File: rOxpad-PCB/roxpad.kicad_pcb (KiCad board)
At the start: 2 copper layers, 66 x 53 mm, 8 parts

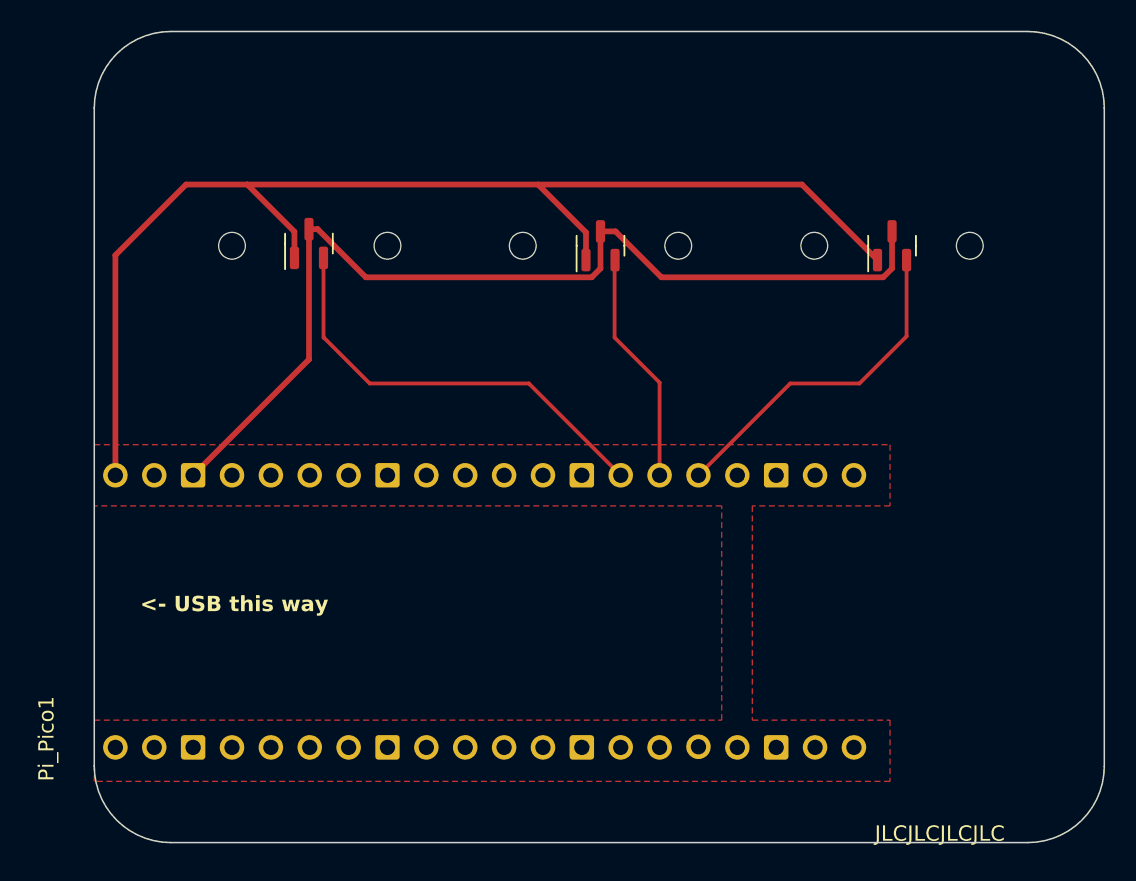
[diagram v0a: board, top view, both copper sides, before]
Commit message: fix pinout (thanks Bexin!)
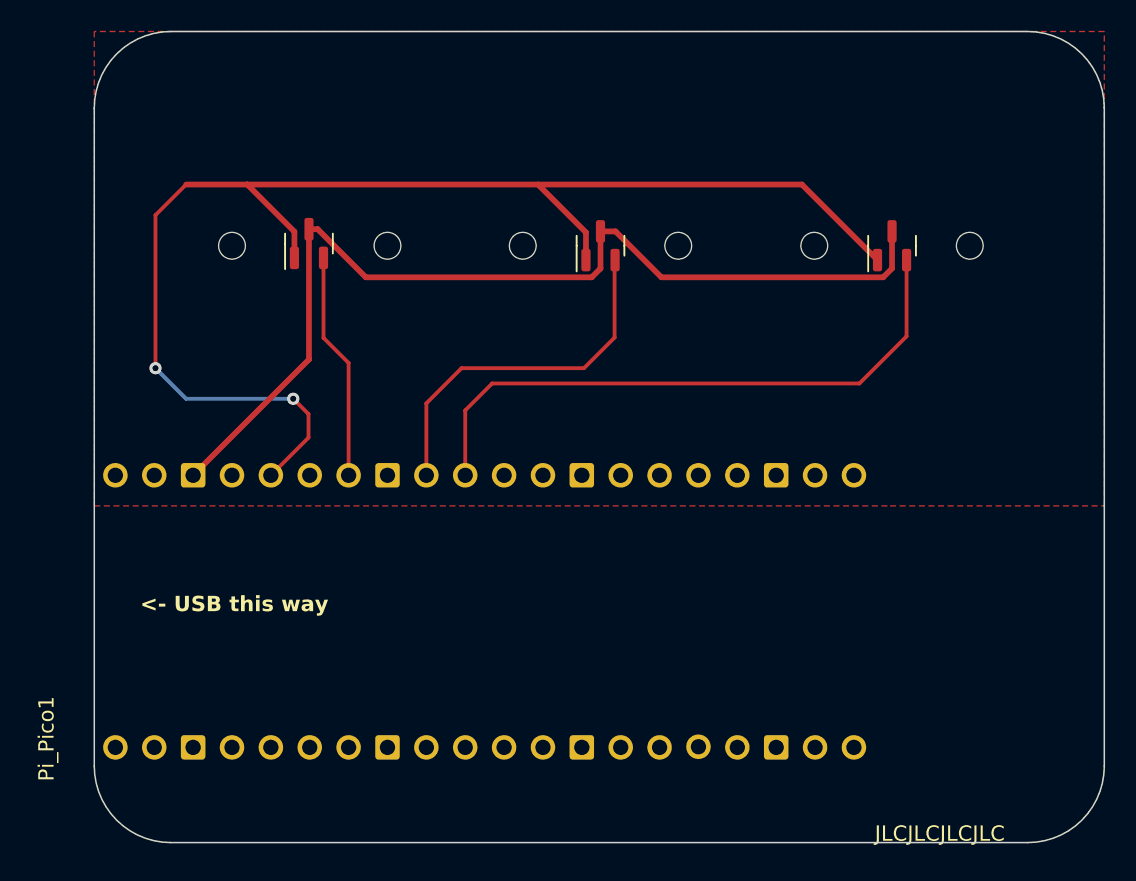
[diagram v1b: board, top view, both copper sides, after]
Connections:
- Pi_Pico1 pad 25: Net-(Pi_Pico1-GP19) -> unconnected-(Pi_Pico1-GP19-Pad25)
- Pi_Pico1 pad 26: Net-(Middle_Sensor1-OUT) -> unconnected-(Pi_Pico1-GP20-Pad26)
- Pi_Pico1 pad 27: Net-(Left_sensor1-OUT) -> unconnected-(Pi_Pico1-GP21-Pad27)
- Pi_Pico1 pad 31: unconnected-(Pi_Pico1-GP26-Pad31) -> Net-(Pi_Pico1-GP26)
- Pi_Pico1 pad 32: unconnected-(Pi_Pico1-GP27-Pad32) -> Net-(Middle_Sensor1-OUT)
- Pi_Pico1 pad 34: unconnected-(Pi_Pico1-GP28-Pad34) -> Net-(Left_sensor1-OUT)
- Pi_Pico1 pad 36: unconnected-(Pi_Pico1-3V3_OUT-Pad36) -> Net-(Left_sensor1-VDD)
- Pi_Pico1 pad 40: Net-(Left_sensor1-VDD) -> unconnected-(Pi_Pico1-VBUS-Pad40)
- Right_Sensor1 pad 2: Net-(Pi_Pico1-GP19) -> Net-(Pi_Pico1-GP26)
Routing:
- net Net-(Pi_Pico1-GP26): track 0.00 -> 40.1 mm
- net Net-(Pi_Pico1-GP19): track 22.3 -> 0.00 mm
- net Net-(Left_sensor1-OUT): track 28.4 -> 14.9 mm
- net Net-(Middle_Sensor1-OUT): track 15.3 -> 23.9 mm
- net Net-(Left_sensor1-VDD): track 80.4 -> 88.6 mm, vias 0 -> 2
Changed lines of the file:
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@@
   (net 30 "unconnected-(Pi_Pico1-GP22-Pad29)")
   (net 31 "unconnected-(Pi_Pico1-RUN-Pad30)")
-  (net 32 "unconnected-(Pi_Pico1-GP26-Pad31)")
-  (net 33 "unconnected-(Pi_Pico1-GP27-Pad32)")
+  (net 32 "unconnected-(Pi_Pico1-GP19-Pad25)")
+  (net 33 "unconnected-(Pi_Pico1-GP20-Pad26)")
   (net 34 "unconnected-(Pi_Pico1-AGND-Pad33)")
-  (net 35 "unconnected-(Pi_Pico1-GP28-Pad34)")
+  (net 35 "unconnected-(Pi_Pico1-GP21-Pad27)")
   (net 36 "unconnected-(Pi_Pico1-ADC_VREF-Pad35)")
-  (net 37 "unconnected-(Pi_Pico1-3V3_OUT-Pad36)")
-  (net 38 "Net-(Pi_Pico1-GP19)")
-  (net 39 "unconnected-(Pi_Pico1-VSYS-Pad39)")
+  (net 37 "Net-(Pi_Pico1-GP26)")
+  (net 38 "unconnected-(Pi_Pico1-VSYS-Pad39)")
+  (net 39 "unconnected-(Pi_Pico1-VBUS-Pad40)")
   (net 40 "unconnected-(Pi_Pico1-3V3_EN-Pad37)")
   (footprint "marbastlib-mx:SW_MX_1u_lekker" (layer "F.Cu")
@@
       (net 25 "unconnected-(Pi_Pico1-GP18-Pad24)") (pinfunction "GP18") (pintype "bidirectional"))
     (pad "25" thru_hole circle (at 8.89 13.97 90) (size 1.6 1.6) (drill 1) (layers "*.Cu" "*.Mask")
-      (net 38 "Net-(Pi_Pico1-GP19)") (pinfunction "GP19") (pintype "bidirectional"))
+      (net 32 "unconnected-(Pi_Pico1-GP19-Pad25)") (pinfunction "GP19") (pintype "bidirectional"))
     (pad "26" thru_hole circle (at 8.89 11.43 90) (size 1.6 1.6) (drill 1) (layers "*.Cu" "*.Mask")
-      (net 4 "Net-(Middle_Sensor1-OUT)") (pinfunction "GP20") (pintype "bidirectional"))
+      (net 33 "unconnected-(Pi_Pico1-GP20-Pad26)") (pinfunction "GP20") (pintype "bidirectional"))
     (pad "27" thru_hole circle (at 8.89 8.89 90) (size 1.6 1.6) (drill 1) (layers "*.Cu" "*.Mask")
-      (net 2 "Net-(Left_sensor1-OUT)") (pinfunction "GP21") (pintype "bidirectional"))
+      (net 35 "unconnected-(Pi_Pico1-GP21-Pad27)") (pinfunction "GP21") (pintype "bidirectional"))
     (pad "28" thru_hole roundrect (at 8.89 6.35 90) (size 1.6 1.6) (drill 1) (layers "*.Cu" "*.Mask") (roundrect_rratio 0.125)
       (net 29 "unconnected-(Pi_Pico1-GND-Pad28)") (pinfunction "GND") (pintype "power_in"))
@@
       (net 31 "unconnected-(Pi_Pico1-RUN-Pad30)") (pinfunction "RUN") (pintype "input"))
     (pad "31" thru_hole circle (at 8.89 -1.27 90) (size 1.6 1.6) (drill 1) (layers "*.Cu" "*.Mask")
-      (net 32 "unconnected-(Pi_Pico1-GP26-Pad31)") (pinfunction "GP26") (pintype "bidirectional"))
+      (net 37 "Net-(Pi_Pico1-GP26)") (pinfunction "GP26") (pintype "bidirectional"))
     (pad "32" thru_hole circle (at 8.89 -3.81 90) (size 1.6 1.6) (drill 1) (layers "*.Cu" "*.Mask")
-      (net 33 "unconnected-(Pi_Pico1-GP27-Pad32)") (pinfunction "GP27") (pintype "bidirectional"))
+      (net 4 "Net-(Middle_Sensor1-OUT)") (pinfunction "GP27") (pintype "bidirectional"))
     (pad "33" thru_hole roundrect (at 8.89 -6.35 90) (size 1.6 1.6) (drill 1) (layers "*.Cu" "*.Mask") (roundrect_rratio 0.125)
       (net 34 "unconnected-(Pi_Pico1-AGND-Pad33)") (pinfunction "AGND") (pintype "power_in"))
     (pad "34" thru_hole circle (at 8.89 -8.89 90) (size 1.6 1.6) (drill 1) (layers "*.Cu" "*.Mask")
-      (net 35 "unconnected-(Pi_Pico1-GP28-Pad34)") (pinfunction "GP28") (pintype "bidirectional"))
+      (net 2 "Net-(Left_sensor1-OUT)") (pinfunction "GP28") (pintype "bidirectional"))
     (pad "35" thru_hole circle (at 8.89 -11.43 90) (size 1.6 1.6) (drill 1) (layers "*.Cu" "*.Mask")
       (net 36 "unconnected-(Pi_Pico1-ADC_VREF-Pad35)") (pinfunction "ADC_VREF") (pintype "power_in"))
     (pad "36" thru_hole circle (at 8.89 -13.97 90) (size 1.6 1.6) (drill 1) (layers "*.Cu" "*.Mask")
-      (net 37 "unconnected-(Pi_Pico1-3V3_OUT-Pad36)") (pinfunction "3V3_OUT") (pintype "power_in"))
+      (net 1 "Net-(Left_sensor1-VDD)") (pinfunction "3V3_OUT") (pintype "power_in"))
     (pad "37" thru_hole circle (at 8.89 -16.51 90) (size 1.6 1.6) (drill 1) (layers "*.Cu" "*.Mask")
       (net 40 "unconnected-(Pi_Pico1-3V3_EN-Pad37)") (pinfunction "3V3_EN") (pintype "input"))
@@
       (net 3 "Net-(Left_sensor1-GND)") (pinfunction "GND") (pintype "power_in"))
     (pad "39" thru_hole circle (at 8.89 -21.59 90) (size 1.6 1.6) (drill 1) (layers "*.Cu" "*.Mask")
-      (net 39 "unconnected-(Pi_Pico1-VSYS-Pad39)") (pinfunction "VSYS") (pintype "free"))
+      (net 38 "unconnected-(Pi_Pico1-VSYS-Pad39)") (pinfunction "VSYS") (pintype "free"))
     (pad "40" thru_hole circle (at 8.89 -24.13 90) (size 1.6 1.6) (drill 1) (layers "*.Cu" "*.Mask")
-      (net 1 "Net-(Left_sensor1-VDD)") (pinfunction "VBUS") (pintype "free"))
+      (net 39 "unconnected-(Pi_Pico1-VBUS-Pad40)") (pinfunction "VBUS") (pintype "free"))
     (model "${KICAD6_3DMODEL_USER_DIR}/RPi Pico w_headers.step"
       (offset (xyz 0 0 9))
@@
       (net 1 "Net-(Left_sensor1-VDD)") (pinfunction "VDD") (pintype "power_in"))
     (pad "2" smd roundrect (at -0.9375 0.95 90) (size 1.475 0.6) (layers "F.Cu" "F.Paste" "F.Mask") (roundrect_rratio 0.25)
-      (net 38 "Net-(Pi_Pico1-GP19)") (pinfunction "OUT") (pintype "output"))
+      (net 37 "Net-(Pi_Pico1-GP26)") (pinfunction "OUT") (pintype "output"))
     (pad "3" smd roundrect (at 0.9375 0 90) (size 1.475 0.6) (layers "F.Cu" "F.Paste" "F.Mask") (roundrect_rratio 0.25)
       (net 3 "Net-(Left_sensor1-GND)") (pinfunction "GND") (pintype "power_in"))
@@
     (effects (font (size 1 1) (thickness 0.15)) (justify left bottom))
   )
+  (segment (start 163 56) (end 163 66) (width 0.25) (layer "F.Cu") (net 1))
+  (segment (start 172 68) (end 173 69) (width 0.25) (layer "F.Cu") (net 1))
   (segment (start 169 54) (end 205.2425 54) (width 0.375) (layer "F.Cu") (net 1))
+  (segment (start 165 54) (end 163 56) (width 0.25) (layer "F.Cu") (net 1))
   (segment (start 191.13 57.13) (end 188 54) (width 0.375) (layer "F.Cu") (net 1))
   (segment (start 172.08 57.08) (end 169 54) (width 0.375) (layer "F.Cu") (net 1))
   (segment (start 165 54) (end 169 54) (width 0.375) (layer "F.Cu") (net 1))
-  (segment (start 160.38 73) (end 160.38 58.62) (width 0.375) (layer "F.Cu") (net 1))
-  (segment (start 160.38 58.62) (end 165 54) (width 0.375) (layer "F.Cu") (net 1))
   (segment (start 191.13 58.9375) (end 191.13 57.13) (width 0.375) (layer "F.Cu") (net 1))
   (segment (start 172.08 58.793749) (end 172.08 57.08) (width 0.375) (layer "F.Cu") (net 1))
+  (segment (start 173 69) (end 173 70.54) (width 0.25) (layer "F.Cu") (net 1))
   (segment (start 205.2425 54) (end 210.18 58.9375) (width 0.375) (layer "F.Cu") (net 1))
-  (segment (start 193.4 73) (end 187.4 67) (width 0.25) (layer "F.Cu") (net 2))
+  (segment (start 173 70.54) (end 170.54 73) (width 0.25) (layer "F.Cu") (net 1))
+  (via (at 163 66) (size 0.8) (drill 0.4) (layers "F.Cu" "B.Cu") (net 1))
+  (via (at 172 68) (size 0.8) (drill 0.4) (layers "F.Cu" "B.Cu") (net 1))
+  (segment (start 163 66) (end 165 68) (width 0.25) (layer "B.Cu") (net 1))
+  (segment (start 165 68) (end 172 68) (width 0.25) (layer "B.Cu") (net 1))
   (segment (start 173.98 58.793749) (end 173.98 64.02) (width 0.25) (layer "F.Cu") (net 2))
-  (segment (start 177 67) (end 174 64) (width 0.25) (layer "F.Cu") (net 2))
-  (segment (start 187.4 67) (end 177 67) (width 0.25) (layer "F.Cu") (net 2))
+  (segment (start 173.98 64.02) (end 175.62 65.66) (width 0.25) (layer "F.Cu") (net 2))
+  (segment (start 175.62 65.66) (end 175.62 73) (width 0.25) (layer "F.Cu") (net 2))
   (segment (start 211.13 57.0625) (end 211.13 59.48514) (width 0.375) (layer "F.Cu") (net 3))
   (segment (start 173.03 56.918749) (end 173.03 65.43) (width 0.375) (layer "F.Cu") (net 3))
@@
   (segment (start 173.60264 56.918749) (end 173.03 56.918749) (width 0.375) (layer "F.Cu") (net 3))
   (segment (start 191.50264 60.0625) (end 176.746391 60.0625) (width 0.375) (layer "F.Cu") (net 3))
+  (segment (start 191 66) (end 183 66) (width 0.25) (layer "F.Cu") (net 4))
   (segment (start 193 58.9675) (end 193 64) (width 0.25) (layer "F.Cu") (net 4))
   (segment (start 193.03 58.9375) (end 193 58.9675) (width 0.25) (layer "F.Cu") (net 4))
-  (segment (start 195.94 73) (end 195.94 66.94) (width 0.25) (layer "F.Cu") (net 4))
-  (segment (start 195.94 66.94) (end 193 64) (width 0.25) (layer "F.Cu") (net 4))
-  (segment (start 204.48 67) (end 198.48 73) (width 0.25) (layer "F.Cu") (net 38))
-  (segment (start 212.08 58.9375) (end 212.08 63.92) (width 0.25) (layer "F.Cu") (net 38))
-  (segment (start 209 67) (end 204.48 67) (width 0.25) (layer "F.Cu") (net 38))
-  (segment (start 212.08 63.92) (end 209 67) (width 0.25) (layer "F.Cu") (net 38))
+  (segment (start 180.7 68.3) (end 180.7 73) (width 0.25) (layer "F.Cu") (net 4))
+  (segment (start 183 66) (end 180.7 68.3) (width 0.25) (layer "F.Cu") (net 4))
+  (segment (start 193 64) (end 191 66) (width 0.25) (layer "F.Cu") (net 4))
+  (segment (start 209 67) (end 185 67) (width 0.25) (layer "F.Cu") (net 37))
+  (segment (start 185 67) (end 183.24 68.76) (width 0.25) (layer "F.Cu") (net 37))
+  (segment (start 212.08 63.92) (end 209 67) (width 0.25) (layer "F.Cu") (net 37))
+  (segment (start 183.24 68.76) (end 183.24 73) (width 0.25) (layer "F.Cu") (net 37))
+  (segment (start 212.08 58.9375) (end 212.08 63.92) (width 0.25) (layer "F.Cu") (net 37))
   (zone (net 3) (net_name "Net-(Left_sensor1-GND)") (layer "F.Cu") (hatch edge 0.5)
     (connect_pads (clearance 0.5))
     (min_thickness 0.25) (filled_areas_thickness no)
-    (fill (thermal_gap 0.5) (thermal_bridge_width 0.5))
+    (fill yes (thermal_gap 0.5) (thermal_bridge_width 0.5))
     (polygon
       (pts
-        (xy 159 71)
-        (xy 211 71)
+        (xy 159 75)
         (xy 211 75)
-        (xy 202 75)
-        (xy 202 89)
-        (xy 211 89)
-        (xy 211 93)
-        (xy 159 93)
-        (xy 159 89)
-        (xy 200 89)
-        (xy 200 75)
-        (xy 159 75)
-      )
-    )
+        (xy 225 75)
+        (xy 225 71)
+        (xy 225 44)
+        (xy 159 44)
+      )
+    )

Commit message: change ' hall sensor`to proper sensor name
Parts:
- Left_sensor1, Middle_Sensor1, Right_Sensor1: value Hall_Sensor -> SS49E
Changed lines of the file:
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@@
         (effects (font (size 1 1) (thickness 0.15)))
     )
-    (fp_text value "Hall_Sensor" (at 0 2.4 90) (layer "F.Fab")
+    (fp_text value "SS49E" (at 0 2.4 90) (layer "F.Fab")
         (effects (font (size 1 1) (thickness 0.15)))
     )
@@
         (effects (font (size 1 1) (thickness 0.15)))
     )
-    (fp_text value "Hall_Sensor" (at 0 2.4 90) (layer "F.Fab")
+    (fp_text value "SS49E" (at 0 2.4 90) (layer "F.Fab")
         (effects (font (size 1 1) (thickness 0.15)))
     )
@@
         (effects (font (size 1 1) (thickness 0.15)))
     )
-    (fp_text value "Hall_Sensor" (at 0 2.4 90) (layer "F.Fab")
+    (fp_text value "SS49E" (at 0 2.4 90) (layer "F.Fab")
         (effects (font (size 1 1) (thickness 0.15)))
     )
@@
     (effects (font (size 1 1) (thickness 0.15)) (justify left bottom))
   )
+  (dimension (type aligned) (layer "Cmts.User")
+    (pts (xy 170 97) (xy 170 44))
+    (height -19)
+    (gr_text "53.0000 mm" (at 149.2 70.5 90) (layer "Cmts.User")
+      (effects (font (size 1.5 1.5) (thickness 0.3)))
+    )
+    (format (prefix "") (suffix "") (units 3) (units_format 1) (precision 4))
+    (style (thickness 0.2) (arrow_length 1.27) (text_position_mode 0) (extension_height 0.58642) (extension_offset 0.5) keep_text_aligned)
+  )
+  (dimension (type aligned) (layer "Cmts.User")
+    (pts (xy 163.555 58) (xy 220.655 58))
+    (height -11)
+    (gr_text "57.1000 mm" (at 192.105 45.2) (layer "Cmts.User")
+      (effects (font (size 1.5 1.5) (thickness 0.3)))
+    )
+    (format (prefix "") (suffix "") (units 3) (units_format 1) (precision 4))
+    (style (thickness 0.2) (arrow_length 1.27) (text_position_mode 0) (extension_height 0.58642) (extension_offset 0.5) keep_text_aligned)
+  )
+  (dimension (type aligned) (layer "Cmts.User")
+    (pts (xy 159 50) (xy 225 50))
+    (height -13)
+    (gr_text "66.0000 mm" (at 192 35.85) (layer "Cmts.User")
+      (effects (font (size 1 1) (thickness 0.15)))
+    )
+    (format (prefix "") (suffix "") (units 3) (units_format 1) (precision 4))
+    (style (thickness 0.15) (arrow_length 1.27) (text_position_mode 0) (extension_height 0.58642) (extension_offset 0.5) keep_text_aligned)
+  )
   (segment (start 163 56) (end 163 66) (width 0.25) (layer "F.Cu") (net 1))

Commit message: changed designations
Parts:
- renumbered Left_sensor1 to H1, Middle_Sensor1 to H2, Right_Sensor1 to H3
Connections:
- Pi_Pico1 pad 31: Net-(Pi_Pico1-GP26) -> Net-(H3-OUT)
- Pi_Pico1 pad 32: Net-(Middle_Sensor1-OUT) -> Net-(H2-OUT)
- Pi_Pico1 pad 34: Net-(Left_sensor1-OUT) -> Net-(H1-OUT)
- Pi_Pico1 pad 36: Net-(Left_sensor1-VDD) -> Net-(H1-VDD)
- Pi_Pico1 pad 38: Net-(Left_sensor1-GND) -> Net-(H1-GND)
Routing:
- added copper zone on F.Cu, net Net-(H1-GND)
- removed copper zone on F.Cu, net Net-(Left_sensor1-GND)
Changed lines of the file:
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@@
       (outputformat 1)
       (mirror false)
-      (drillshape 1)
+      (drillshape 0)
       (scaleselection 1)
-      (outputdirectory "")
+      (outputdirectory "gerber/")
     )
   )
@@
   (net 39 "unconnected-(Pi_Pico1-VBUS-Pad40)")
   (net 40 "unconnected-(Pi_Pico1-3V3_EN-Pad37)")
+  (net 41 "Net-(H1-VDD)")
+  (net 42 "Net-(H1-OUT)")
+  (net 43 "Net-(H1-GND)")
+  (net 44 "Net-(H2-OUT)")
+  (net 45 "Net-(H3-OUT)")
   (footprint "marbastlib-mx:SW_MX_1u_lekker" (layer "F.Cu")
     (at 173.08 58)
@@
       (net 31 "unconnected-(Pi_Pico1-RUN-Pad30)") (pinfunction "RUN") (pintype "input"))
     (pad "31" thru_hole circle (at 8.89 -1.27 90) (size 1.6 1.6) (drill 1) (layers "*.Cu" "*.Mask")
-      (net 37 "Net-(Pi_Pico1-GP26)") (pinfunction "GP26") (pintype "bidirectional"))
+      (net 45 "Net-(H3-OUT)") (pinfunction "GP26") (pintype "bidirectional"))
     (pad "32" thru_hole circle (at 8.89 -3.81 90) (size 1.6 1.6) (drill 1) (layers "*.Cu" "*.Mask")
-      (net 4 "Net-(Middle_Sensor1-OUT)") (pinfunction "GP27") (pintype "bidirectional"))
+      (net 44 "Net-(H2-OUT)") (pinfunction "GP27") (pintype "bidirectional"))
     (pad "33" thru_hole roundrect (at 8.89 -6.35 90) (size 1.6 1.6) (drill 1) (layers "*.Cu" "*.Mask") (roundrect_rratio 0.125)
       (net 34 "unconnected-(Pi_Pico1-AGND-Pad33)") (pinfunction "AGND") (pintype "power_in"))
     (pad "34" thru_hole circle (at 8.89 -8.89 90) (size 1.6 1.6) (drill 1) (layers "*.Cu" "*.Mask")
-      (net 2 "Net-(Left_sensor1-OUT)") (pinfunction "GP28") (pintype "bidirectional"))
+      (net 42 "Net-(H1-OUT)") (pinfunction "GP28") (pintype "bidirectional"))
     (pad "35" thru_hole circle (at 8.89 -11.43 90) (size 1.6 1.6) (drill 1) (layers "*.Cu" "*.Mask")
       (net 36 "unconnected-(Pi_Pico1-ADC_VREF-Pad35)") (pinfunction "ADC_VREF") (pintype "power_in"))
     (pad "36" thru_hole circle (at 8.89 -13.97 90) (size 1.6 1.6) (drill 1) (layers "*.Cu" "*.Mask")
-      (net 1 "Net-(Left_sensor1-VDD)") (pinfunction "3V3_OUT") (pintype "power_in"))
+      (net 41 "Net-(H1-VDD)") (pinfunction "3V3_OUT") (pintype "power_in"))
     (pad "37" thru_hole circle (at 8.89 -16.51 90) (size 1.6 1.6) (drill 1) (layers "*.Cu" "*.Mask")
       (net 40 "unconnected-(Pi_Pico1-3V3_EN-Pad37)") (pinfunction "3V3_EN") (pintype "input"))
     (pad "38" thru_hole roundrect (at 8.89 -19.05 90) (size 1.6 1.6) (drill 1) (layers "*.Cu" "*.Mask") (roundrect_rratio 0.125)
-      (net 3 "Net-(Left_sensor1-GND)") (pinfunction "GND") (pintype "power_in"))
+      (net 43 "Net-(H1-GND)") (pinfunction "GND") (pintype "power_in"))
     (pad "39" thru_hole circle (at 8.89 -21.59 90) (size 1.6 1.6) (drill 1) (layers "*.Cu" "*.Mask")
       (net 38 "unconnected-(Pi_Pico1-VSYS-Pad39)") (pinfunction "VSYS") (pintype "free"))
@@
     (property "ki_keywords" "linear analog hall effect magnetic")
     (attr smd)
-    (fp_text reference "Middle_Sensor1" (at 0 -2.4 90) (layer "F.SilkS") hide
+    (fp_text reference "H2" (at 0 -2.4 90) (layer "F.SilkS") hide
         (effects (font (size 1 1) (thickness 0.15)))
     )
@@
     (property "ki_keywords" "linear analog hall effect magnetic")
     (attr smd)
-    (fp_text reference "Right_Sensor1" (at 0 -2.4 90) (layer "F.SilkS") hide
+    (fp_text reference "H3" (at 0 -2.4 90) (layer "F.SilkS") hide
         (effects (font (size 1 1) (thickness 0.15)))
     )
@@
     (property "ki_keywords" "linear analog hall effect magnetic")
     (attr smd)
-    (fp_text reference "Left_sensor1" (at 0 -2.4 90) (layer "F.SilkS") hide
+    (fp_text reference "H1" (at 0 -2.4 90) (layer "F.SilkS") hide
         (effects (font (size 1 1) (thickness 0.15)))
     )
@@
   (segment (start 183.24 68.76) (end 183.24 73) (width 0.25) (layer "F.Cu") (net 37))
   (segment (start 212.08 58.9375) (end 212.08 63.92) (width 0.25) (layer "F.Cu") (net 37))
-  (zone (net 3) (net_name "Net-(Left_sensor1-GND)") (layer "F.Cu") (hatch edge 0.5)
+  (zone (net 43) (net_name "Net-(H1-GND)") (layer "F.Cu") (hatch edge 0.5)
     (connect_pads (clearance 0.5))
     (min_thickness 0.25) (filled_areas_thickness no)
